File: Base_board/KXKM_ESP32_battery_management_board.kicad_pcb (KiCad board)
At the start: 2 copper layers, 56.5 x 57.5 mm, 99 parts, among them J1 Conn_01x06, J11 TEST_1P, J13 Wire pad, J14 Wire pad, J15 Wire pad, J16 Wire pad, J2 TEST_1P, J3 Conn_02x10_Odd_Even, J4 Conn_01x04, J5 Micro_SD_Card, J6 Conn_01x03, J7 Conn_01x03, J8 Conn_01x03, J9 USB_A, P1 TC_SWD, Q1 BC847W, Q2 BC847W, Q4 2N7002, Q5 2N7002, Q6 2N7002, SW1 SW_Push, SW3 SW_Push, SW4 SW_SP3T, U1 ESP32-WROOM, U2 SP3485CN, U3 MCP16331T-E/CH, U4 BTS50080-1TEA, U5 DC_DC_POL, U7 STM32F030F4Px

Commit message: Fix component values > pick n place convention
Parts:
- C10, C9: value 10uF,10V -> 10uF
- C4, C5: value 10uF,50V -> 10uF/50V
- D11, D3: value 100V,1A -> 1A/100V
- D13, D2: value Zener,3V,300mW -> Zener/3V/300mW
- F1: value 30V,0.5A -> 0.5A/30V
- R1, R10, R28: value 10k,1% -> 10k/1%
- R12, R22: value 1k,1% -> 1k/1%
- R15: value 270k,1% -> 270k/1%
- R16, R9: value 31.6k,1% -> 31.6k/1%
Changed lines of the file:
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@@
   )
   (layers
-    (0 F.Cu signal hide)
+    (0 F.Cu signal)
     (31 B.Cu signal hide)
     (32 B.Adhes user hide)
@@
       (effects (font (size 1 1) (thickness 0.15)) (justify mirror))
     )
-    (fp_text value 10uF,10V (at 0 -1.65 270) (layer B.Fab) hide
+    (fp_text value 10uF (at 0 -1.65 270) (layer B.Fab) hide
       (effects (font (size 1 1) (thickness 0.15)) (justify mirror))
     )
@@
       (effects (font (size 1 1) (thickness 0.15)) (justify mirror))
     )
-    (fp_text value 31.6k,1% (at 0 -1.43 270) (layer B.Fab) hide
+    (fp_text value 31.6k/1% (at 0 -1.43 270) (layer B.Fab) hide
       (effects (font (size 1 1) (thickness 0.15)) (justify mirror))
     )
@@
       (effects (font (size 1 1) (thickness 0.15)) (justify mirror))
     )
-    (fp_text value 10k,1% (at 0 -1.43 90) (layer B.Fab) hide
+    (fp_text value 10k/1% (at 0 -1.43 90) (layer B.Fab) hide
       (effects (font (size 1 1) (thickness 0.15)) (justify mirror))
     )
@@
       (effects (font (size 1 1) (thickness 0.15)) (justify mirror))
     )
-    (fp_text value 10k,1% (at 0 -1.43 180) (layer B.Fab) hide
+    (fp_text value 10k/1% (at 0 -1.43 180) (layer B.Fab) hide
       (effects (font (size 1 1) (thickness 0.15)) (justify mirror))
     )
@@
       (effects (font (size 1 1) (thickness 0.15)) (justify mirror))
     )
-    (fp_text value Zener,3V,300mW (at 0.1 -1.9 180) (layer B.Fab) hide
+    (fp_text value Zener/3V/300mW (at 0.1 -1.9 180) (layer B.Fab) hide
       (effects (font (size 1 1) (thickness 0.15)) (justify mirror))
     )
@@
       (effects (font (size 1 1) (thickness 0.15)) (justify mirror))
     )
-    (fp_text value 1k,1% (at 0 -1.43 270) (layer B.Fab) hide
+    (fp_text value 1k/1% (at 0 -1.43 270) (layer B.Fab) hide
       (effects (font (size 1 1) (thickness 0.15)) (justify mirror))
     )
@@
       (effects (font (size 1 1) (thickness 0.15)) (justify mirror))
     )
-    (fp_text value 100V,1A (at 0 -2.6 180) (layer B.Fab) hide
+    (fp_text value 1A/100V (at 0 -2.6 180) (layer B.Fab) hide
       (effects (font (size 1 1) (thickness 0.15)) (justify mirror))
     )
@@
       (effects (font (size 1 1) (thickness 0.15)) (justify mirror))
     )
-    (fp_text value 10uF,10V (at 0 -1.65) (layer B.Fab) hide
+    (fp_text value 10uF (at 0 -1.65) (layer B.Fab) hide
       (effects (font (size 1 1) (thickness 0.15)) (justify mirror))
     )
@@
       (effects (font (size 1 1) (thickness 0.15)) (justify mirror))
     )
-    (fp_text value 10uF,50V (at 0 -1.82 180) (layer B.Fab) hide
+    (fp_text value 10uF/50V (at 0 -1.82 180) (layer B.Fab) hide
       (effects (font (size 1 1) (thickness 0.15)) (justify mirror))
     )
@@
       (effects (font (size 1 1) (thickness 0.15)) (justify mirror))
     )
-    (fp_text value 10uF,50V (at 0 -1.82 180) (layer B.Fab) hide
+    (fp_text value 10uF/50V (at 0 -1.82 180) (layer B.Fab) hide
       (effects (font (size 1 1) (thickness 0.15)) (justify mirror))
     )
@@
       (effects (font (size 1 1) (thickness 0.15)) (justify mirror))
     )
-    (fp_text value Zener,3V,300mW (at 0.1 -1.9 180) (layer B.Fab) hide
+    (fp_text value Zener/3V/300mW (at 0.1 -1.9 180) (layer B.Fab) hide
       (effects (font (size 1 1) (thickness 0.15)) (justify mirror))
     )
@@
       (effects (font (size 1 1) (thickness 0.15)) (justify mirror))
     )
-    (fp_text value 10k,1% (at 0 -1.43 270) (layer B.Fab) hide
+    (fp_text value 10k/1% (at 0 -1.43 270) (layer B.Fab) hide
       (effects (font (size 1 1) (thickness 0.15)) (justify mirror))
     )
@@
       (effects (font (size 1 1) (thickness 0.15)) (justify mirror))
     )
-    (fp_text value 1k,1% (at 0 -1.43 270) (layer B.Fab) hide
+    (fp_text value 1k/1% (at 0 -1.43 270) (layer B.Fab) hide
       (effects (font (size 1 1) (thickness 0.15)) (justify mirror))
     )
@@
       (effects (font (size 1 1) (thickness 0.15)) (justify mirror))
     )
-    (fp_text value 270k,1% (at 0 -1.43 180) (layer B.Fab) hide
+    (fp_text value 270k/1% (at 0 -1.43 180) (layer B.Fab) hide
       (effects (font (size 1 1) (thickness 0.15)) (justify mirror))
     )
@@
       (effects (font (size 1 1) (thickness 0.15)) (justify mirror))
     )
-    (fp_text value 31.6k,1% (at 0 -1.43) (layer B.Fab) hide
+    (fp_text value 31.6k/1% (at 0 -1.43) (layer B.Fab) hide
       (effects (font (size 1 1) (thickness 0.15)) (justify mirror))
     )
@@
       (effects (font (size 1 1) (thickness 0.15)) (justify mirror))
     )
-    (fp_text value 100V,1A (at 0 -2.6 90) (layer B.Fab) hide
+    (fp_text value 1A/100V (at 0 -2.6 90) (layer B.Fab) hide
       (effects (font (size 1 1) (thickness 0.15)) (justify mirror))
     )
@@
       (effects (font (size 1 1) (thickness 0.15)) (justify mirror))
     )
-    (fp_text value 30V,0.5A (at 0 -2.65) (layer B.Fab) hide
+    (fp_text value 0.5A/30V (at 0 -2.65) (layer B.Fab) hide
       (effects (font (size 1 1) (thickness 0.15)) (justify mirror))
     )

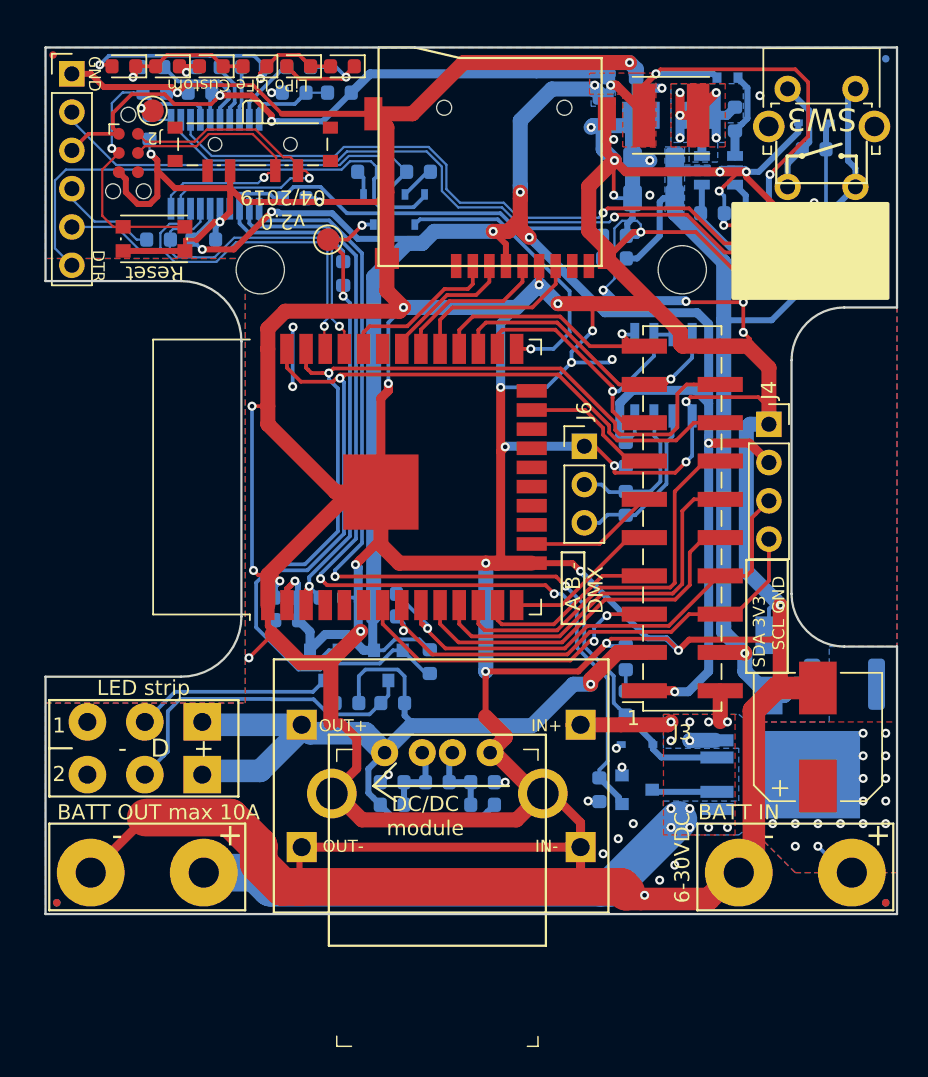
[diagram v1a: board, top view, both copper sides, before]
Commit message: First look at v3 : components on top side only. Board area maximised for
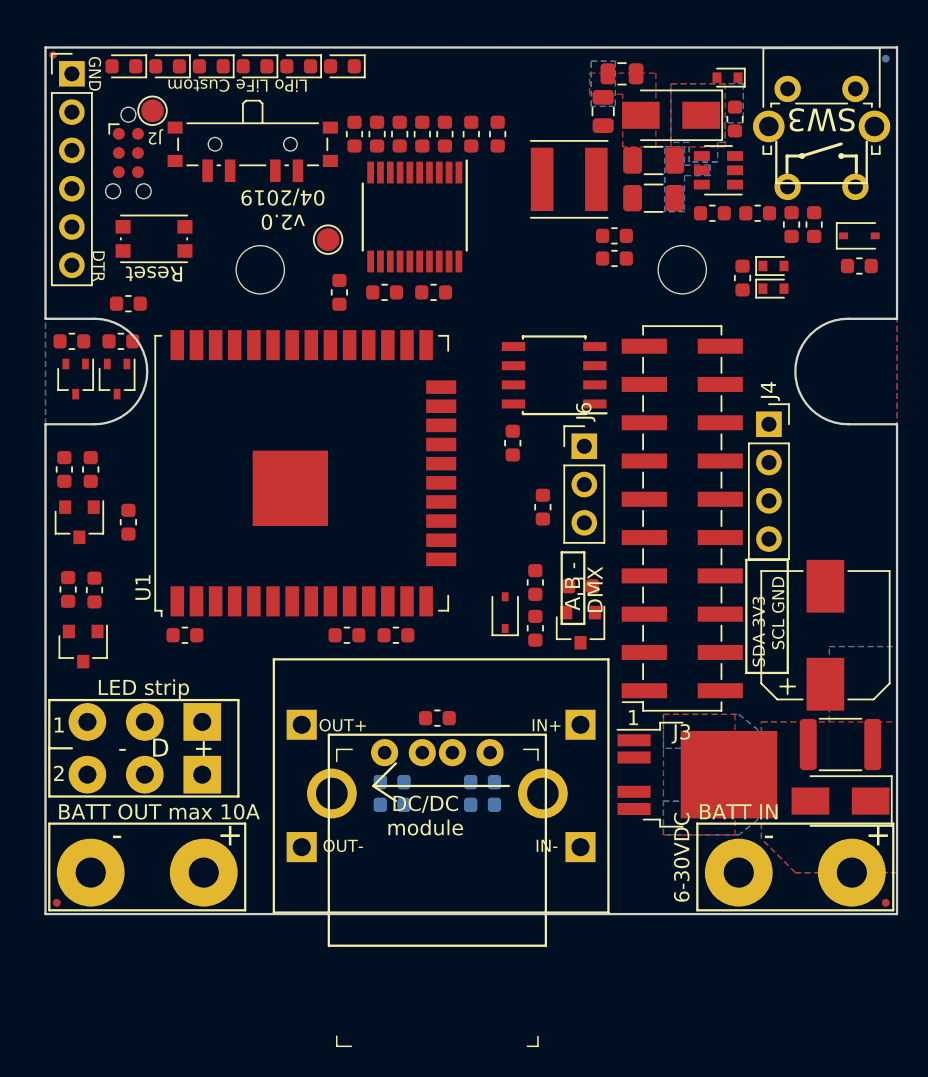
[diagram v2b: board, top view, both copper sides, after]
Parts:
- removed J5: Micro_SD_Card, tom_kicad_lib:microSD-Receptacle-SelfEject
- removed R28: 10k/1%, Resistor_SMD:R_0603_1608Metric
- removed TH1: Thermistor_NTC, Resistor_SMD:R_0603_1608Metric
- C1, C10, C2, C21, C22, C23, C24, C26, C3, C4, C5, C7, C8, C9, D1, D11, D12, D13, D2, D3, D4, F1, Q1, Q2, Q4, Q5, Q6, R1, R10, R11, R12, R15, R16, R17, R18, R19, R2, R20, R21, R22, R23, R24, R25, R26, R27, R3, R31, R4, R5, R6, R7, R8, R9, U2, U3, U4, U7: moved to F.Cu
- U1: footprint RF_Module:ESP32-WROOM-32 -> RF_Module:ESP32-WROOM-32U
- moved R5 25.6 mm to (104.8, 100.0), turned to 0 degrees
- moved Q1 25.2 mm to (105.0, 102.5)
- moved R23 23.1 mm to (133.0, 86.2), turned to 90 degrees
- moved R20 22.8 mm to (104.5, 116.5), turned to 90 degrees
- moved R18 22.8 mm to (106.2, 116.5), turned to 270 degrees
- moved C24 21.2 mm to (131.2, 86.2), turned to 90 degrees
- moved Q2 20.4 mm to (107.8, 102.5)
- moved Q5 20.3 mm to (105.5, 120.2)
- moved R6 20.0 mm to (108.0, 100.0), turned to 180 degrees
- moved Q4 18.8 mm to (105.2, 112.0)
- moved R19 18.8 mm to (108.5, 112.0), turned to 90 degrees
- moved R26 18.5 mm to (128.0, 86.2), turned to 270 degrees
- moved C1 18.1 mm to (106.0, 108.5), turned to 270 degrees
- moved R17 17.8 mm to (104.2, 108.5), turned to 270 degrees
- moved C22 16.5 mm to (129.5, 86.2), turned to 90 degrees
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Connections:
- SW4 pad : GND -> (no net)
- U1 pad 29: /SD_DO -> Net-(U1-Pad29)
- U1 pad 30: /SD_SCK -> Net-(U1-Pad30)
- U1 pad 31: /SD_DI -> Net-(U1-Pad31)
- U1 pad 33: /SD_CS -> Net-(U1-Pad33)
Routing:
- net GND: track 605.8 -> 0.00 mm, vias 61 -> 0
- net +3V3: track 226.4 -> 0.00 mm, vias 14 -> 0
- net +BATT: track 72.7 -> 0.00 mm, vias 1 -> 0
- net /LED_DATA_2: track 68.2 -> 0.00 mm, vias 1 -> 0
- net /Battery monitoring/LOAD_I_SENSE: track 63.9 -> 0.00 mm, vias 2 -> 0
- net /Battery monitoring/MAIN_OUT_EN: track 63.9 -> 0.00 mm, vias 2 -> 0
- net VBUS: track 62.4 -> 0.00 mm, vias 1 -> 0
- net /Battery monitoring/EN_PUSH_BUTTON: track 61.1 -> 0.00 mm, vias 2 -> 0
- net /LED_DATA_1: track 59.6 -> 0.00 mm, vias 1 -> 0
- net /Battery monitoring/3.3V_EN: track 46.7 -> 0.00 mm, vias 2 -> 0
- net +VSW: track 44.1 -> 0.00 mm, vias 12 -> 0
- net /I2C_SCL: track 34.8 -> 0.00 mm, vias 1 -> 0
- net /PROG_DTR: track 34.7 -> 0.00 mm
- net /I2C_SDA: track 32.7 -> 0.00 mm, vias 1 -> 0
- net /ESP32_EN: track 31.2 -> 0.00 mm, vias 3 -> 0
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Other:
- outline, holes or cut-outs redrawn
- board text added: "+3.3V"
- board text added: "2x diam. 3mm"
- board text added: "A"
- board text added: "B"
- board text added: "D1"
- board text added: "D2"
- board text added: "DMX / RS485"
- board text added: "Ecran OLED"
- board text added: "Entrée batterie"
- board text added: "Extension"
- board text added: "Inter. On/Off déporté"
- board text added: "SCL"
- board text added: "SDA"
- board text added: "Sortie de puissance commandée"

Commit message: cleaning and moving components
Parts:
- added REF**: SW_DIP_SPSTx03_Piano_CTS_Series194-3MSTN_W7.62mm_P2.54mm, Button_Switch_THT:SW_DIP_SPSTx03_Piano_CTS_Series194-3MSTN_W7.62mm_P2.54mm, F.Cu at (133.8, 81.8)
- moved J2 14.5 mm to (124.4, 87.0)
- moved R11 12.4 mm to (134.6, 99.6), turned to 0 degrees
- moved R24 12.4 mm to (124.3, 98.7), turned to 0 degrees
- moved R25 10.9 mm to (124.3, 97.2), turned to 0 degrees
- moved J11 10.6 mm to (112.3, 98.0)
- moved R5 10.6 mm to (108.0, 110.1), turned to 270 degrees
- moved C21 10.0 mm to (135.5, 97.2), turned to 270 degrees
- moved R27 9.65 mm to (124.3, 95.7), turned to 0 degrees
- moved Q2 9.22 mm to (105.3, 111.4), turned to 180 degrees
- moved R23 9.17 mm to (124.3, 89.2), turned to 180 degrees
- moved R26 8.72 mm to (124.3, 94.2), turned to 0 degrees
- moved J7 8.38 mm to (105.5, 122.6), turned to 270 degrees
- moved C24 8.36 mm to (124.3, 90.9), turned to 180 degrees
- moved C22 8.25 mm to (124.3, 92.7), turned to 180 degrees
- moved J8 7.60 mm to (109.0, 122.6), turned to 270 degrees
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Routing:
- removed copper zone on B.Cu, net +3V3
- removed copper zone on F.Cu, net +3V3
- removed copper zone on B.Cu, net +BATT
- removed copper zone on B.Cu, net Net-(C7-Pad2)
- removed copper zone on F.Cu, net Net-(C7-Pad2)
